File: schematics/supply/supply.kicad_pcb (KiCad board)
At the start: 4 copper layers, 110 x 175 mm, 230 parts, among them J1 Conn_01x02_Pin, J10 USBASP, J11 USBASP, J12 Conn_01x06_Pin, J14 Conn_01x05_Pin, J15 banana jack + fuse 15A, J16 banana jack + fuse 15A, J2 Conn_01x01_Pin, J20 Conn_02x04_Odd_Even, J21 jst xh angle, J22 jst xh angle, J3 USB_A, J4 USB_A, J5 USB_A, J6 Conn_01x04_Pin, J8 Conn_01x04_Pin, M1 Fan, Q1 40N06, Q10 IRLML0030, Q11 IRLML5203, Q12 IRLML5203, Q2 STP13NK60Z, Q3 STP13NK60Z, Q4 IRLML0030, Q5 IRLML5203, Q6 IRLML5203, Q7 IRLML0030, Q8 IRLML0030, Q9 IRLML0030, SW3 SW_Push, U1 INA3221, U10 LM158DR, U11 LM1085-3.3, U12 ATmega328-A, U13 ATtiny1616-M, U15 LM158DR, U16 EL817, U17 IRS2153S, U18 TL331, U19 INA169, U2 EL817, U20 TP4056, U21 INA3221, U3 MC34063AD, U4 L78L33ACUTR, U5 IRS2153S, U6 LM158DR, U7 IP2163, U8 LM158DR, U9 TL432DBZ, X1 HC-49U, 16MHz, X2 CSX-750FCC, 16MHz

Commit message: Found and fixed issues in schematics.
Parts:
- added R64: 0.01, Resistor_SMD:R_2512_6332Metric, F.Cu at (105.4, 169.8)
- C7: value 0.33 uF -> 10 uF
- C9: value 100 nF -> 10 uF
- R10, R45, R46, R9: value 5 -> 10
- R13, R18, R23, R24: value 1K -> 510
- R47: value 70K -> 68K
- R48: value 30K -> 33K
- R51: value 1K -> 680
- R6: value 1K -> 50
- TR2: value ETD 49/25/16@N87 N19@1mm*2/7+7@1mm*4 -> ETD 49/25/16@N87 N18@1mm*2/7+7@1mm*4
- U5: value IRS2153S -> IR2153S
- X2: value CSX-750FCC, 16MHz -> 16MHz, SMD3225
- moved R6 9.21 mm to (97.5, 185.2), turned to 180 degrees
- moved C1 2.53 mm to (107.0, 191.0), turned to 180 degrees
- moved C2 1.42 mm to (102.7, 181.5), turned to -90 degrees
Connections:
- L1 pad 1: /Internal 5V & out usb/USB_1_+5V -> Net-(U3-DC)
- U3 pad 1: /Internal 5V & out usb/USB_1_+5V -> Net-(U3-DC)
- U3 pad 7: /Internal 5V & out usb/USB_1_+5V -> Net-(U3-DC)
- U3 pad 8: /Internal 5V & out usb/USB_1_+5V -> Net-(U3-DC)
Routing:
- net Net-(U3-DC): track 0.00 -> 69.8 mm, vias 0 -> 2
- net /Internal 5V & out usb/USB_1_+5V: track 51.6 -> 32.7 mm
- net Net-(Q1-G): track 17.3 -> 15.0 mm
- net Net-(U3-TC): track 2.88 -> 3.65 mm

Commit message: Some changes
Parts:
- C21, C4, C41: value 100 nF -> 1 uF
- C23, C24, C25, C26, C29, C31, C32, C33: value 100 nF -> 220 nF
- C34, C35, C36, C37: value 1 uF -> 220 nF
- R1: value 510 -> 120
- R17: value 10K -> 3K3
- R2: value 1K2 -> NOT INSTALLED
- R30: value 100K -> 10K
- R33: value 200K -> 10K
- R35, R36: value 5K -> 5K1
- R53: value 49K5 -> 47K
- R6: value 50 -> 51
- R62: value 2K -> 510
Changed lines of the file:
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@@
         (effects (font (size 1 1) (thickness 0.15)) (justify mirror))
     )
-    (fp_text value "100 nF" (at 0 -1.43) (layer "B.Fab")
+    (fp_text value "220 nF" (at 0 -1.43) (layer "B.Fab")
         (effects (font (size 1 1) (thickness 0.15)) (justify mirror))
     )
@@
         (effects (font (size 1 1) (thickness 0.15)) (justify mirror))
     )
-    (fp_text value "100 nF" (at 0 -1.43 90) (layer "B.Fab")
+    (fp_text value "1 uF" (at 0 -1.43 90) (layer "B.Fab")
         (effects (font (size 1 1) (thickness 0.15)) (justify mirror))
     )
@@
         (effects (font (size 1 1) (thickness 0.15)) (justify mirror))
     )
-    (fp_text value "100 nF" (at 0 -1.43) (layer "B.Fab")
+    (fp_text value "220 nF" (at 0 -1.43) (layer "B.Fab")
         (effects (font (size 1 1) (thickness 0.15)) (justify mirror))
     )
@@
         (effects (font (size 1 1) (thickness 0.15)) (justify mirror))
     )
-    (fp_text value "10K" (at 0 -1.65 90) (layer "B.Fab")
+    (fp_text value "3K3" (at 0 -1.65 90) (layer "B.Fab")
         (effects (font (size 1 1) (thickness 0.15)) (justify mirror))
     )
@@
         (effects (font (size 1 1) (thickness 0.15)) (justify mirror))
     )
-    (fp_text value "1K2" (at 0 -1.65 90) (layer "B.Fab")
+    (fp_text value "NOT INSTALLED" (at 0 -1.65 90) (layer "B.Fab")
         (effects (font (size 1 1) (thickness 0.15)) (justify mirror))
     )
@@
         (effects (font (size 1 1) (thickness 0.15)) (justify mirror))
     )
-    (fp_text value "5K" (at 0 -1.65 90) (layer "B.Fab")
+    (fp_text value "5K1" (at 0 -1.65 90) (layer "B.Fab")
         (effects (font (size 1 1) (thickness 0.15)) (justify mirror))
     )
@@
         (effects (font (size 1 1) (thickness 0.15)) (justify mirror))
     )
-    (fp_text value "50" (at 0 -1.65) (layer "B.Fab")
+    (fp_text value "51" (at 0 -1.65) (layer "B.Fab")
         (effects (font (size 1 1) (thickness 0.15)) (justify mirror))
     )
@@
         (effects (font (size 1 1) (thickness 0.15)) (justify mirror))
     )
-    (fp_text value "100 nF" (at 0 -1.43 90) (layer "B.Fab")
+    (fp_text value "220 nF" (at 0 -1.43 90) (layer "B.Fab")
         (effects (font (size 1 1) (thickness 0.15)) (justify mirror))
     )
@@
         (effects (font (size 1 1) (thickness 0.15)) (justify mirror))
     )
-    (fp_text value "49K5" (at 0 -1.65 90) (layer "B.Fab")
+    (fp_text value "47K" (at 0 -1.65 90) (layer "B.Fab")
         (effects (font (size 1 1) (thickness 0.15)) (justify mirror))
     )
@@
         (effects (font (size 1 1) (thickness 0.15)) (justify mirror))
     )
-    (fp_text value "5K" (at 0 -1.65 90) (layer "B.Fab")
+    (fp_text value "5K1" (at 0 -1.65 90) (layer "B.Fab")
         (effects (font (size 1 1) (thickness 0.15)) (justify mirror))
     )
@@
         (effects (font (size 1 1) (thickness 0.15)) (justify mirror))
     )
-    (fp_text value "1 uF" (at 0 -1.43 90) (layer "B.Fab")
+    (fp_text value "220 nF" (at 0 -1.43 90) (layer "B.Fab")
         (effects (font (size 1 1) (thickness 0.15)) (justify mirror))
     )
@@
         (effects (font (size 1 1) (thickness 0.15)) (justify mirror))
     )
-    (fp_text value "100 nF" (at 0 -1.43 90) (layer "B.Fab")
+    (fp_text value "1 uF" (at 0 -1.43 90) (layer "B.Fab")
         (effects (font (size 1 1) (thickness 0.15)) (justify mirror))
     )
@@
         (effects (font (size 1 1) (thickness 0.15)) (justify mirror))
     )
-    (fp_text value "100 nF" (at 0 -1.43) (layer "B.Fab")
+    (fp_text value "220 nF" (at 0 -1.43) (layer "B.Fab")
         (effects (font (size 1 1) (thickness 0.15)) (justify mirror))
     )
@@
         (effects (font (size 1 1) (thickness 0.15)) (justify mirror))
     )
-    (fp_text value "100 nF" (at 0 -1.43) (layer "B.Fab")
+    (fp_text value "1 uF" (at 0 -1.43) (layer "B.Fab")
         (effects (font (size 1 1) (thickness 0.15)) (justify mirror))
     )
@@
         (effects (font (size 1 1) (thickness 0.15)) (justify mirror))
     )
-    (fp_text value "100 nF" (at 0 -1.43) (layer "B.Fab")
+    (fp_text value "220 nF" (at 0 -1.43) (layer "B.Fab")
         (effects (font (size 1 1) (thickness 0.15)) (justify mirror))
     )
@@
         (effects (font (size 1 1) (thickness 0.15)) (justify mirror))
     )
-    (fp_text value "510" (at 0 -1.65) (layer "B.Fab")
+    (fp_text value "120" (at 0 -1.65) (layer "B.Fab")
         (effects (font (size 1 1) (thickness 0.15)) (justify mirror))
     )
@@
         (effects (font (size 1 1) (thickness 0.15)) (justify mirror))
     )
-    (fp_text value "100 nF" (at 0 -1.43) (layer "B.Fab")
+    (fp_text value "220 nF" (at 0 -1.43) (layer "B.Fab")
         (effects (font (size 1 1) (thickness 0.15)) (justify mirror))
     )
@@
         (effects (font (size 1 1) (thickness 0.15)) (justify mirror))
     )
-    (fp_text value "1 uF" (at 0 -1.43 90) (layer "B.Fab")
+    (fp_text value "220 nF" (at 0 -1.43 90) (layer "B.Fab")
         (effects (font (size 1 1) (thickness 0.15)) (justify mirror))
     )
@@
         (effects (font (size 1 1) (thickness 0.15)) (justify mirror))
     )
-    (fp_text value "1 uF" (at 0 -1.43 90) (layer "B.Fab")
+    (fp_text value "220 nF" (at 0 -1.43 90) (layer "B.Fab")
         (effects (font (size 1 1) (thickness 0.15)) (justify mirror))
     )
@@
         (effects (font (size 1 1) (thickness 0.15)) (justify mirror))
     )
-    (fp_text value "1 uF" (at 0 -1.43 90) (layer "B.Fab")
+    (fp_text value "220 nF" (at 0 -1.43 90) (layer "B.Fab")
         (effects (font (size 1 1) (thickness 0.15)) (justify mirror))
     )
@@
         (effects (font (size 1 1) (thickness 0.15)) (justify mirror))
     )
-    (fp_text value "100K" (at 0 -1.65) (layer "B.Fab")
+    (fp_text value "10K" (at 0 -1.65) (layer "B.Fab")
         (effects (font (size 1 1) (thickness 0.15)) (justify mirror))
     )
@@
         (effects (font (size 1 1) (thickness 0.15)) (justify mirror))
     )
-    (fp_text value "2K" (at 0 -1.65) (layer "B.Fab")
+    (fp_text value "510" (at 0 -1.65) (layer "B.Fab")
         (effects (font (size 1 1) (thickness 0.15)) (justify mirror))
     )
@@
         (effects (font (size 1 1) (thickness 0.15)) (justify mirror))
     )
-    (fp_text value "200K" (at 0 -1.65 90) (layer "B.Fab")
+    (fp_text value "10K" (at 0 -1.65 90) (layer "B.Fab")
         (effects (font (size 1 1) (thickness 0.15)) (justify mirror))
     )
@@
         (effects (font (size 1 1) (thickness 0.15)) (justify mirror))
     )
-    (fp_text value "100 nF" (at 0 -1.43) (layer "B.Fab")
+    (fp_text value "220 nF" (at 0 -1.43) (layer "B.Fab")
         (effects (font (size 1 1) (thickness 0.15)) (justify mirror))
     )
@@
         (effects (font (size 1 1) (thickness 0.15)) (justify mirror))
     )
-    (fp_text value "100 nF" (at 0 -1.43) (layer "B.Fab")
+    (fp_text value "220 nF" (at 0 -1.43) (layer "B.Fab")
         (effects (font (size 1 1) (thickness 0.15)) (justify mirror))
     )

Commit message: Continue soldering and setting up hardware
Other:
- board text added: "Supply board#2 v1.1"
- board text removed: "Supply board#2 v1.0"
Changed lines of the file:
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@@
     (fp_line (start 3.15 1.6) (end -3.15 1.6)
       (stroke (width 0.1) (type solid)) (layer "F.Fab"))
-    (pad "1" smd roundrect (at -2.9625 0 180) (size 1.225 3.35) (layers "F.Cu" "F.Paste" "F.Mask") (roundrect_rratio 0.204082)
+    (pad "1" smd roundrect (at -2.9625 0 180) (size 1.225 3.35) (layers "F.Cu" "F.Paste" "F.Mask") (roundrect_rratio 0.2040816327)
       (net 6 "/Internal 5V & out usb/USB_1_+5V") (pintype "passive"))
-    (pad "2" smd roundrect (at 2.9625 0 180) (size 1.225 3.35) (layers "F.Cu" "F.Paste" "F.Mask") (roundrect_rratio 0.204082)
+    (pad "2" smd roundrect (at 2.9625 0 180) (size 1.225 3.35) (layers "F.Cu" "F.Paste" "F.Mask") (roundrect_rratio 0.2040816327)
       (net 157 "Net-(U3-DC)") (pintype "passive"))
     (model "${KICAD6_3DMODEL_DIR}/Resistor_SMD.3dshapes/R_2512_6332Metric.wrl"
@@
   (gr_line (start 196.5 239.75) (end 86.5 239.75)
     (stroke (width 0.15) (type default)) (layer "User.4"))
-  (gr_text "Supply board#2 v1.0" (at 116.5 63.8) (layer "B.SilkS")
+  (gr_text "Supply board#2 v1.1" (at 116.5 63.8) (layer "B.SilkS")
     (effects (font (size 1.5 1.5) (thickness 0.3) bold) (justify left bottom mirror))
   )

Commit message: Board fixes
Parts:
- added R65: 0.07, Resistor_SMD:R_2512_6332Metric, F.Cu at (105.3, 171.8)
- added R66: 0.07, Resistor_SMD:R_2512_6332Metric, F.Cu at (105.3, 175.9)
- D1, D20: value SS16 -> STTH1R06A
- R64: value 0.01 -> 0.07
- moved R64 2.00 mm to (105.3, 167.8)
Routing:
- net /Internal 5V & out usb/USB_1_+5V: track 32.7 -> 39.7 mm
- net Net-(U3-DC): track 69.8 -> 73.8 mm

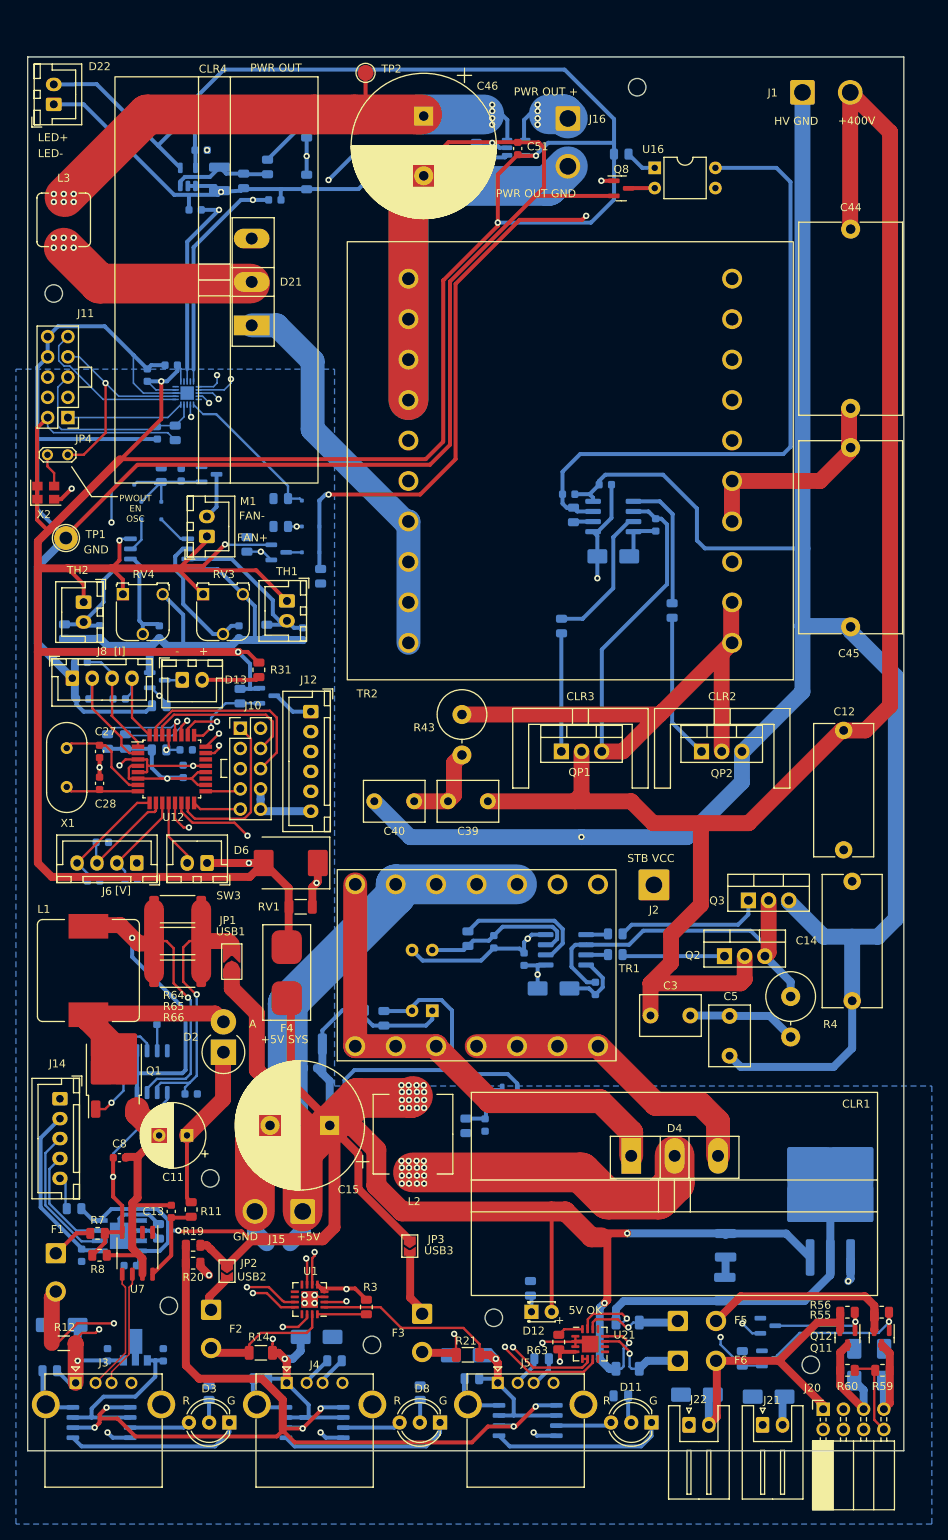
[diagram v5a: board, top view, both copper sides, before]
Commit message: supply board - power controllers changed; PWM logic changed
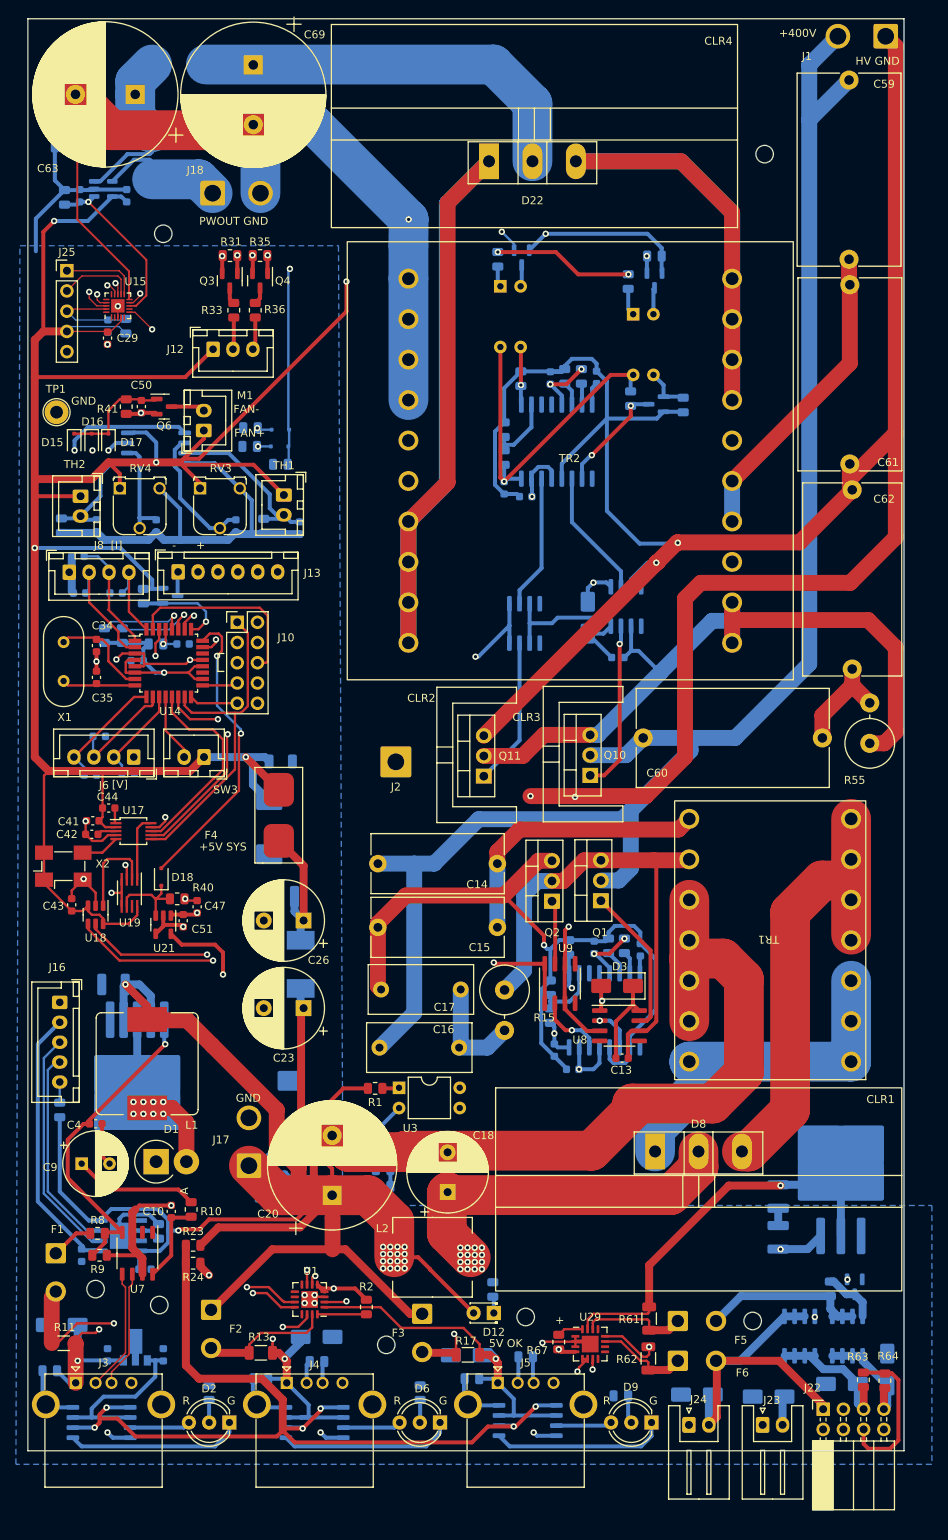
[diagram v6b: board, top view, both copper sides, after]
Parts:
- removed the C10 at (157.8, 177.8)
- removed the C30 at (104.5, 99.5)
- removed the C48 at (108.2, 72.5)
- removed the C6 at (145.0, 171.9)
- removed the D1 at (152.5, 177.8)
- removed D13: GNL-3012ED, Connector_JST:JST_XH_B2B-XH-A_1x02_P2.50mm_Vertical
- removed D14: BAV21WS, Diode_SMD:D_SOD-323F
- removed the D20 at (160.0, 123.5)
- removed the D22 at (89.8, 66.8)
- removed J11: USBASP, Connector_PinHeader_2.54mm:PinHeader_2x05_P2.54mm_Vertical
- removed JP1: SolderJumper_2_Open, Library:SolderedJumper-2P-2mm
- removed JP2, JP3: SolderJumper_2_Open, Jumper:SolderJumper-2_P1.3mm_Open_TrianglePad1.0x1.5mm
- removed JP4: Jumper_2_Open, TestPoint:TestPoint_2Pads_Pitch2.54mm_Drill0.8mm
- removed the Q1 at (97.3, 187.9)
- removed the Q12 at (189.4, 221.6)
- removed the Q6 at (118.0, 123.0)
- removed QP1, QP2: STP13NK60Z, Package_TO_SOT_THT:TO-220-3_Vertical
- removed the R10 at (160.2, 170.9)
- removed the R2 at (131.2, 181.5)
- removed the R37 at (114.0, 122.0)
- removed the R42 at (161.0, 73.0)
- removed the R44 at (155.0, 118.3)
- removed the R56 at (189.4, 218.4)
- removed the R64 at (105.3, 167.8)
- removed the R65 at (105.3, 171.8)
- removed the R66 at (105.3, 175.9)
- removed the R9 at (160.2, 173.5)
- removed TP2: POWER_OUTPUT, TestPoint:TestPoint_Pad_D2.0mm
- removed U16: EL817, Package_DIP:DIP-4_W7.62mm
- removed the U3 at (102.1, 188.2)
- added C13: 1 uF, Capacitor_SMD:C_0603_1608Metric, F.Cu at (161.1, 186.5)
- added C19: 22 uF, Capacitor_SMD:C_1210_3225Metric, B.Cu at (142.2, 200.8)
- added C23: 1000 uF@16V, Capacitor_THT:CP_Radial_D10.0mm_P5.00mm, F.Cu at (121.1, 180.2)
- added C25: 22 uF, Capacitor_SMD:C_1210_3225Metric, B.Cu at (118.5, 166.2)
- added C26: 1000 uF@16V, Capacitor_THT:CP_Radial_D10.0mm_P5.00mm, F.Cu at (121.1, 169.2)
- added C44: 10 nF, Capacitor_SMD:C_0603_1608Metric, F.Cu at (96.7, 155.1)
- added C5: 2 nF, Capacitor_SMD:C_0603_1608Metric, B.Cu at (157.6, 172.6)
- added C51: 1 uF, Capacitor_SMD:C_0603_1608Metric, F.Cu at (106.0, 169.2)
- added C52: 100 nF, Capacitor_SMD:C_0603_1608Metric, B.Cu at (146.3, 114.9)
- added C53: 2 nF, Capacitor_SMD:C_0603_1608Metric, B.Cu at (152.1, 101.1)
- added C54: 100 nF, Capacitor_SMD:C_0603_1608Metric, B.Cu at (157.9, 101.0)
- added C55: 1 uF, Capacitor_SMD:C_0603_1608Metric, B.Cu at (149.0, 116.0)
- added C58: 1 uF, Capacitor_SMD:C_0603_1608Metric, B.Cu at (160.6, 136.2)
- added C69: 2200 uF@63V, Capacitor_THT:CP_Radial_D18.0mm_P7.50mm, F.Cu at (114.8, 61.8)
- added C7: 100 nF, Capacitor_SMD:C_0603_1608Metric, B.Cu at (163.4, 172.9)
- added D18: BAV21WS, Diode_SMD:D_SOD-323F, F.Cu at (103.2, 163.8)
- added D21: STTH1R06A, Diode_SMD:D_SMA, B.Cu at (156.8, 131.2)
- added D3: STTH1R06A, Diode_SMD:D_SMA, F.Cu at (160.5, 177.4)
- added J12: JST XH B3B, Connector_JST:JST_XH_B3B-XH-A_1x03_P2.50mm_Vertical, F.Cu at (109.8, 97.5)
- added J25: Conn_01x05_Socket, Connector_PinHeader_2.54mm:PinHeader_1x05_P2.54mm_Vertical, F.Cu at (91.4, 87.6)
- added L3: 22 uH@0650, Inductor_SMD:L_Chilisin_BMRB00060650, B.Cu at (120.8, 174.7)
- added NT1: NetTie_2, NetTie:NetTie-2_SMD_Pad2.0mm, F.Cu at (108.2, 183.5)
- added NT2: NetTie_2, NetTie:NetTie-2_SMD_Pad2.0mm, F.Cu at (124.8, 208.5)
- added Q13: IRF7425PbF, Package_SO:SOIC-8_3.9x4.9mm_P1.27mm, B.Cu at (189.4, 221.4)
- added Q14: IRF7425PbF, Package_SO:SOIC-8_3.9x4.9mm_P1.27mm, B.Cu at (183.4, 221.4)
- added Q4: IRLML0030, Package_TO_SOT_SMD:SOT-23, F.Cu at (115.7, 88.9)
- added Q7: IRLML0030, Package_TO_SOT_SMD:SOT-23, B.Cu at (148.5, 86.0)
- added Q9: IRLML0030, Package_TO_SOT_SMD:SOT-23, B.Cu at (165.4, 104.4)
- added R19: 100, Resistor_SMD:R_0805_2012Metric, B.Cu at (131.1, 202.6)
- added R3: 10K, Resistor_SMD:R_0805_2012Metric, B.Cu at (152.1, 181.2)
- added R35: 10K, Resistor_SMD:R_0805_2012Metric, F.Cu at (115.7, 85.7)
- added R36: 270, Resistor_SMD:R_0805_2012Metric, F.Cu at (115.0, 92.6)
- added R4: 10K, Resistor_SMD:R_0805_2012Metric, B.Cu at (152.1, 177.7)
- added R40: 1K, Resistor_SMD:R_0805_2012Metric, F.Cu at (105.2, 166.5)
- added R49: 22, Resistor_SMD:R_0805_2012Metric, B.Cu at (156.0, 100.9)
- added R50: 220, Resistor_SMD:R_0805_2012Metric, B.Cu at (161.9, 89.0)
- added R52: 10K, Resistor_SMD:R_0805_2012Metric, B.Cu at (148.4, 101.2)
- added R53: 10K, Resistor_SMD:R_0805_2012Metric, B.Cu at (168.8, 104.5)
- added R7: 22, Resistor_SMD:R_0805_2012Metric, B.Cu at (161.4, 172.4)
- added U19: MAX961, Package_SO:SSOP-8_2.95x2.8mm_P0.65mm, F.Cu at (99.2, 165.8)
- added U2: XL6009, Package_TO_SOT_SMD:TO-263-5_TabPin3, B.Cu at (100.2, 189.3)
- added U21: FAN3100, Package_TO_SOT_SMD:SOT-23-5, F.Cu at (103.5, 169.8)
- added U22: EL817, Package_DIP:DIP-4_W7.62mm, B.Cu at (145.8, 89.6)
- added U23: EL817, Package_DIP:DIP-4_W7.62mm, B.Cu at (162.5, 93.1)
- added U24: UC3525, Package_SO:SOIC-16W_7.5x10.3mm_P1.27mm, B.Cu at (152.9, 109.1)
- added U25: IR2117, Package_SO:SOIC-8_3.9x4.9mm_P1.27mm, B.Cu at (161.6, 129.8)
- added U26: IR2117, Package_SO:SOIC-8_3.9x4.9mm_P1.27mm, B.Cu at (148.9, 131.9)
- added U8: IR2117, Package_SO:SOIC-8_3.9x4.9mm_P1.27mm, F.Cu at (160.8, 182.4)
- added U9: IR2117, Package_SO:SOIC-8_3.9x4.9mm_P1.27mm, F.Cu at (153.3, 177.1)
- C1: value 1 uF -> 100 nF
- C16: renamed from C3; value CK45-B3DD331KYGNA -> К73-17 0.022 uF@630V; footprint Capacitor_THT:C_Disc_D7.5mm_W5.0mm_P5.00mm -> Capacitor_THT:C_Rect_L13.0mm_W6.0mm_P10.00mm_FKS3_FKP3_MKS4
- C17: renamed from C5; value CK45-B3DD331KYGNA -> К73-17 0.022 uF@630V; footprint Capacitor_THT:C_Disc_D7.5mm_W5.0mm_P5.00mm -> Capacitor_THT:C_Rect_L13.0mm_W6.0mm_P10.00mm_FKS3_FKP3_MKS4
- C18: value 10 nF -> 1000 uF@16V; footprint Capacitor_SMD:C_0603_1608Metric -> Capacitor_THT:CP_Radial_D10.0mm_P5.00mm; moved to F.Cu
- C2: value 300 pF -> 22 uF; footprint Capacitor_SMD:C_0603_1608Metric -> Capacitor_SMD:C_1210_3225Metric
- C29: renamed from C22; moved to F.Cu
- C41, C43, R41: moved to F.Cu
- C42: value 470 pF -> 100 nF; moved to F.Cu
- C47: value 22 uF -> 1 uF; footprint Capacitor_SMD:C_1210_3225Metric -> Capacitor_SMD:C_0603_1608Metric; moved to F.Cu
- C50: renamed from C38; moved to F.Cu
- C60: renamed from C39; value CK45-B3DD331KYGNA -> К73-17 0.33 uF@630V; footprint Capacitor_THT:C_Disc_D7.5mm_W5.0mm_P5.00mm -> Capacitor_THT:C_Rect_L24.0mm_W12.2mm_P22.50mm_MKT
- C62: renamed from C40; value CK45-B3DD331KYGNA -> К73-17 0.33 uF@630V; footprint Capacitor_THT:C_Disc_D7.5mm_W5.0mm_P5.00mm -> Capacitor_THT:C_Rect_L24.0mm_W12.2mm_P22.50mm_MKT
- C66: renamed from C51; moved to B.Cu
- D11: renamed from D6; moved to B.Cu
- D15: renamed from D17; moved to F.Cu
- D16: renamed from D18; moved to F.Cu
- D17: renamed from D19; moved to F.Cu
- L4: renamed from L3; moved to B.Cu
- Q10: value IRLML0030 -> STP13NK60Z; footprint Package_TO_SOT_SMD:SOT-23 -> Package_TO_SOT_THT:TO-220-3_Vertical; moved to F.Cu
- Q11: value IRLML5203 -> STP13NK60Z; footprint Package_TO_SOT_SMD:SOT-23 -> Package_TO_SOT_THT:TO-220-3_Vertical
- Q3: renamed from Q4; moved to F.Cu
- Q6: renamed from Q7; moved to F.Cu
- Q8: moved to B.Cu
- R1: value 120 -> 220; moved to F.Cu
- R15: renamed from R4; value 5K1@2W -> 100@2W
- R31: renamed from R30; moved to F.Cu
- R45, R46: value 10 -> 10K
- R47: value 68K -> 5K
- R48: value 33K -> 1K
- R51: value 680 -> 220
- R55: renamed from R43; value 5K1@2W -> 100@2W
- R6: value 51 -> 5K
- R60: renamed from R55; value 10K -> 1K; moved to B.Cu
- R61: renamed from R57; moved to F.Cu
- R62: renamed from R58; moved to F.Cu
- R63: renamed from R59; value 10K -> 1K
- R64: renamed from R60; value 10K -> 1K
- RV2: renamed from RV1; moved to B.Cu
- U15: renamed from U13; moved to F.Cu
- U17: value IRS2153S -> AD9833xRM; footprint Package_SO:SOP-8_3.76x4.96mm_P1.27mm -> Package_SO:MSOP-10_3x3mm_P0.5mm; moved to F.Cu
- U18: value TL331 -> MCP4726A0T-E/CH; footprint Package_TO_SOT_SMD:SOT-23-5 -> Package_TO_SOT_SMD:SOT-23-6; moved to F.Cu
- U3: renamed from U2; moved to F.Cu
- U5: value IR2153S -> UC3525; footprint Package_SO:SOP-8_3.76x4.96mm_P1.27mm -> Package_SO:SOIC-16W_7.5x10.3mm_P1.27mm
- X2: value 16MHz, SMD3225 -> ???; footprint Oscillator:Oscillator_SMD_Abracon_ASE-4Pin_3.2x2.5mm -> Oscillator:Oscillator_SMD_Fordahl_DFAS15-4Pin_5.0x3.2mm_HandSoldering
- moved R54 121.3 mm to (162.2, 103.7)
- moved U18 93.4 mm to (95.0, 168.5), turned to -90 degrees
- moved C47 91.4 mm to (107.8, 167.5)
- moved C43 87.5 mm to (92.0, 167.2), turned to 90 degrees
- moved Q11 86.4 mm to (143.7, 151.1), turned to 90 degrees
- moved C41 77.0 mm to (94.7, 156.7), turned to 180 degrees
- moved C42 73.5 mm to (94.5, 158.4)
- moved Q10 72.6 mm to (157.1, 151.0), turned to 90 degrees
- moved U17 72.0 mm to (99.8, 158.0)
- moved R6 63.2 mm to (159.4, 172.4), turned to 90 degrees
- moved C15 60.3 mm to (130.4, 170.1), turned to 0 degrees
- moved C62 57.5 mm to (190.0, 137.7), turned to 90 degrees
- moved R31 57.2 mm to (111.9, 85.7)
- moved R48 52.4 mm to (165.2, 85.8), turned to 180 degrees
- moved U27 52.1 mm to (96.0, 77.4)
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- renumbered C13 to C10, C12 to C14, C14 to C15, C15 to C20, C16 to C21, C17 to C22, C19 to C24, C20 to C27, C21 to C28, C7 to C3, C23 to C30, C24 to C31, C25 to C32, C26 to C33, C27 to C34, C28 to C35, C29 to C36, C31 to C38, C32 to C39, C8 to C4, C33 to C40, C34 to C45, C35 to C46, C36 to C48, C37 to C49, C44 to C59, C9 to C6, C45 to C61, C46 to C63, C49 to C64, C50 to C65, C52 to C67, C53 to C68, C4 to C8, C11 to C9, D2 to D1, D15 to D19, D3 to D2, D16 to D20, D21 to D22, D5 to D4, D7 to D5, D8 to D6, D9 to D7, D4 to D8, D11 to D9, J12 to J13, J14 to J16, J15 to J17, J16 to J18, J20 to J22, J21 to J23, J22 to J24, Q2 to Q1, Q9 to Q12, Q3 to Q2, R11 to R10, R12 to R11, R13 to R12, R14 to R13, R15 to R14, R18 to R16, R21 to R17, R22 to R18, R3 to R2, R16 to R20, R17 to R21, R23 to R22, R19 to R23, R20 to R24, R24 to R28, R28 to R29, R29 to R30, R31 to R33, R33 to R37, R35 to R38, R36 to R39, R38 to R42, R39 to R43, R40 to R44, R49 to R56, R50 to R57, R52 to R58, R53 to R59, R61 to R65, R62 to R66, R63 to R67, R7 to R8, R8 to R9, RV2 to RV1, U8 to U10, U10 to U11, U9 to U12, U11 to U13, U12 to U14, U15 to U20, U19 to U27, U20 to U28, U21 to U29
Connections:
- C1 pad 1: GND -> /Internal 5V & out usb/DCDC_5V_VREF
- C1 pad 2: /Internal 5V & out usb/USB_1_+5V -> GNDPWR
- C18 pad 1: GND -> Net-(D8-K)
- C18 pad 2: Net-(U9-REF) -> GND
- C2 pad 2: Net-(U3-TC) -> /Internal 5V & out usb/USB_1_+5V
- C36 pad 1: /Control & Fan/POWER_OUTPUT_RESET# -> /Control & Fan/ATTINY_RESET#
- C41 pad 1: GNDPWR -> /Control & Fan/+5V_VSYS
- C41 pad 2: /Internal 5V & out usb/V_STANDBY -> GND
- C42 pad 1: Net-(U17-CT) -> GND
- C42 pad 2: GNDPWR -> Net-(U17-CAP/2.5V)
- C43 pad 1: /Power output/RC_SNABBER_MIDDLEPOINT -> /Control & Fan/+5V_VSYS
- C43 pad 2: Net-(D20-K) -> GND
- C47 pad 1: GND -> /Control & Fan/+5V_VSYS
- C47 pad 2: Net-(U18-+) -> GND
- C63 pad 1: Net-(U19-+) -> Net-(U27-+)
- D1 pad 2: Net-(D2-A) -> Net-(D1-A)
- D8 pad 2: Net-(D4-K) -> Net-(D8-K)
- F2 pad 1: /Internal 5V & out usb/USB_2_+5V -> /Internal 5V & out usb/USB_2_3_+5V
- F3 pad 1: /Internal 5V & out usb/USB_3_+5V -> /Internal 5V & out usb/USB_2_3_+5V
- F4 pad 1: /Internal 5V & out usb/+5V_OUT -> Net-(C25-Pad2)
- J10 pad 4: /Control & Fan/RXD -> unconnected-(J10-Pin_4-Pad4)
- J13 pad 5: /Control & Fan/MISO -> /Control & Fan/TFT_CS
- J22 pad 8: GND -> /Control & Fan/SIGNAL_OUT
- L1 pad 1: Net-(U3-DC) -> Net-(D1-A)
- L1 pad 2: Net-(D2-A) -> /Internal 5V & out usb/USB_1_+5V
- L2 pad 1: Net-(D4-K) -> Net-(D8-K)
- L4 pad 2: Net-(U19-+) -> Net-(U27-+)
- Q10 pad 1: /Control & Fan/SIGNAL_OUT -> Net-(Q10-G)
- Q10 pad 2: GND -> /Internal 5V & out usb/400V
- Q10 pad 3: Net-(Q10-D) -> /Power output/RC_SNABBER_MIDDLEPOINT
- Q11 pad 2: /Output connectors/3.3V_FUSE -> /Power output/RC_SNABBER_MIDDLEPOINT
- Q11 pad 3: /Output connectors/SIGNAL_OUT_PWR_3V3 -> GNDPWR
- Q12 pad 3: Net-(Q11-G) -> Net-(Q12-D)
- Q3 pad 3: Net-(D13-K) -> Net-(Q3-D)
- Q8 pad 1: /Control & Fan/POWER_OUTPUT_FB -> /Control & Fan/POWER_OUTPUT_SHUTDOWN#
- R20 pad 1: /Internal 5V & out usb/+5V_OUT -> Net-(R19-Pad2)
- R20 pad 2: Net-(U9-REF) -> Net-(U12-REF)
- R21 pad 1: Net-(U9-REF) -> Net-(U12-REF)
- R30 pad 1: /Control & Fan/POWER_OUTPUT_RESET# -> /Control & Fan/ATTINY_RESET#
- R33 pad 1: Net-(D13-A) -> Net-(Q3-D)
- R33 pad 2: /Control & Fan/+5V_VSYS -> Net-(J12-Pin_2)
- R45 pad 1: Net-(U17-HO) -> /Power output/DCDC_5V_VREF
- R45 pad 2: Net-(QP1-G) -> /Power output/DCDC_2V5_VREF
- R46 pad 1: Net-(U17-LO) -> /Power output/DCDC_2V5_VREF
- R46 pad 2: Net-(QP2-G) -> GNDPWR
- R47 pad 1: Net-(U18-+) -> Net-(U24-RT)
- R47 pad 2: Net-(U19-+) -> GNDPWR
- R48 pad 1: Net-(U18-+) -> GND
- R48 pad 2: GND -> /Control & Fan/POWER_OUTPUT_SHUTDOWN#
- R5 pad 1: Net-(U5-CT) (its old number) -> /Internal 5V & out usb/DCDC_FEEDBACK
- R5 pad 2: Net-(U5-RT) -> GNDPWR
- R51 pad 1: /Control & Fan/+5V_VSYS -> Net-(R51-Pad1)
- R51 pad 2: Net-(D22-A) -> /Control & Fan/+5V_VSYS
- R54 pad 1: GND -> /Power output/DCDC_5V_VREF
- R54 pad 2: /Control & Fan/SIGNAL_OUT -> /Power output/DCDC_SHUTDOWN
- R56 pad 2: Net-(U19-+) -> Net-(U27-+)
- R58 pad 1: Net-(U19-+) -> Net-(U27-+)
- R6 pad 1: Net-(Q1-G) (its old number) -> Net-(U5-RT)
- R6 pad 2: GND -> GNDPWR
- R60 pad 1: Net-(Q11-G) -> Net-(Q12-D)
- U12 pad 1: Net-(U9-REF) -> Net-(U12-REF)
- U14 pad 13: /Control & Fan/ENABLE_POWER_OUTPUT -> /Control & Fan/SIGNAL_CS
- U14 pad 14: /Control & Fan/SIGNAL_OUT -> /Control & Fan/TFT_CS
- U14 pad 24: /Control & Fan/POWER_OUTPUT_RESET# -> /Control & Fan/SIGNAL_ALWAYS_ON
- U14 pad 30: /Control & Fan/RXD -> /Control & Fan/SIGNAL_GEN_SHTDN
- U15 pad 1: /Control & Fan/ATTINY_MISO -> unconnected-(U15-PA2-Pad1)
- U15 pad 16: /Control & Fan/POWER_OUTPUT_IC_FB -> unconnected-(U15-PC1-Pad16)
- U15 pad 18: unconnected-(U13-PC3-Pad18) -> /Control & Fan/POWER_OUTPUT_VOUT_LED
- U15 pad 19: /Control & Fan/POWER_OUTPUT_RESET# -> /Control & Fan/ATTINY_RESET#
- U15 pad 2: /Control & Fan/ATTINY_SCK -> unconnected-(U15-PA3-Pad2)
- U15 pad 20: /Control & Fan/ATTINY_MOSI -> unconnected-(U15-PA1-Pad20)
- U15 pad 6: /Control & Fan/+5V_VSYS -> /Control & Fan/POWER_OUTPUT_IC_FB
- U15 pad 9: unconnected-(U13-PB5-Pad9) -> /Control & Fan/POWER_OUTPUT_SHUTDOWN#
- U17 pad 1: /Internal 5V & out usb/V_STANDBY -> Net-(U17-COMP)
- U17 pad 2: Net-(U17-RT) -> /Control & Fan/+5V_VSYS
- U17 pad 3: Net-(U17-CT) -> Net-(U17-CAP/2.5V)
- U17 pad 4: GNDPWR -> GND
- U17 pad 5: Net-(U17-LO) -> Net-(U17-MCLK)
- U17 pad 6: /Power output/RC_SNABBER_MIDDLEPOINT -> /Control & Fan/MOSI
- U17 pad 7: Net-(U17-HO) -> /Control & Fan/SCK
- U17 pad 8: Net-(D20-K) -> /Control & Fan/SIGNAL_CS
- U18 pad 1: GND -> Net-(U18-VOUT)
- U18 pad 3: Net-(U18-+) -> /Control & Fan/+5V_VSYS
- U18 pad 4: Net-(D22-A) -> /Control & Fan/SDA
- U18 pad 5: /Control & Fan/+5V_VSYS -> /Control & Fan/SCL
- U27 pad 3: Net-(U19-+) -> Net-(U27-+)
- U3 pad 3: GNDPWR -> /Internal 5V & out usb/DCDC_FEEDBACK
- U3 pad 4: Net-(U5-CT) (its old number) -> /Internal 5V & out usb/DCDC_5V_VREF
- U5 pad 1: /Internal 5V & out usb/V_STANDBY -> /Internal 5V & out usb/DCDC_FEEDBACK
- U5 pad 2: Net-(U5-RT) -> /Internal 5V & out usb/DCDC_2V5_VREF
- U5 pad 3: Net-(U5-CT) (its old number) -> unconnected-(U5-SYNC-Pad3)
- U5 pad 4: GNDPWR -> unconnected-(U5-OSC-Pad4)
- U5 pad 6: /Internal 5V & out usb/RC_SNABBER_MIDDLEPOINT -> Net-(U5-RT)
- X2 pad 3: Net-(JP4-B) -> Net-(U17-MCLK)
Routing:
- net GND: track 935.6 -> 591.0 mm, vias 15 -> 23
- net Net-(U19-+): track 152.3 -> 0.00 mm, vias 10 -> 0
- net GNDPWR: track 326.2 -> 457.9 mm, vias 2 -> 6
- net Net-(D4-K): track 115.5 -> 0.00 mm, vias 16 -> 0
- net /Internal 5V & out usb/V_STANDBY: track 78.3 -> 171.8 mm, vias 2 -> 6
- net Net-(D8-K): track 0.00 -> 91.9 mm, vias 0 -> 16
- net /Control & Fan/POWER_OUTPUT_RESET#: track 84.1 -> 0.00 mm, vias 1 -> 0
- net Net-(U17-CT): track 81.6 -> 0.00 mm
- net /Control & Fan/+5V_VSYS: track 718.8 -> 640.2 mm, vias 13 -> 14
- net Net-(U3-DC): track 73.8 -> 0.00 mm, vias 2 -> 0
- net /Control & Fan/POWER_OUTPUT_SHUTDOWN#: track 0.00 -> 69.6 mm, vias 0 -> 2
- net Net-(D22-A-Pad3): track 155.3 -> 91.7 mm
- net /Control & Fan/SCL: track 179.6 -> 228.2 mm, vias 4 -> 5
- net /Control & Fan/ENABLE_POWER_OUTPUT: track 47.7 -> 0.00 mm, vias 2 -> 0
- net /Power output/DCDC_5V_VREF: track 0.00 -> 45.0 mm, vias 0 -> 1
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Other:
- board size 110 x 175 mm -> 110 x 179.8 mm
- board text added: "PWOUT GND"
- board text removed: "+5V"
- board text removed: "LED+"
- board text removed: "LED-"
- board text removed: "PWOUT EN OSC"
- board text removed: "PWR OUT"
- board text removed: "PWR OUT +"
- board text removed: "PWR OUT GND"
- board text removed: "STB VCC"
- board text removed: "USB1"
- board text removed: "USB2"
- board text removed: "USB3"
